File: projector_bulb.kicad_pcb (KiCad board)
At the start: 2 copper layers, 85.7 x 85.7 mm, 45 parts, among them J1 to_upright_+, J2 to_upright_-, J3 to_base, J4 Conn_02x02_Odd_Even, J5 Conn_02x02_Odd_Even, U1 PAM2863, U2 AP7381-33Y

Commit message: Added fillets after much blood sweat and tears
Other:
- board size 85.7 x 85.7 mm -> 85.7 x 85.6 mm

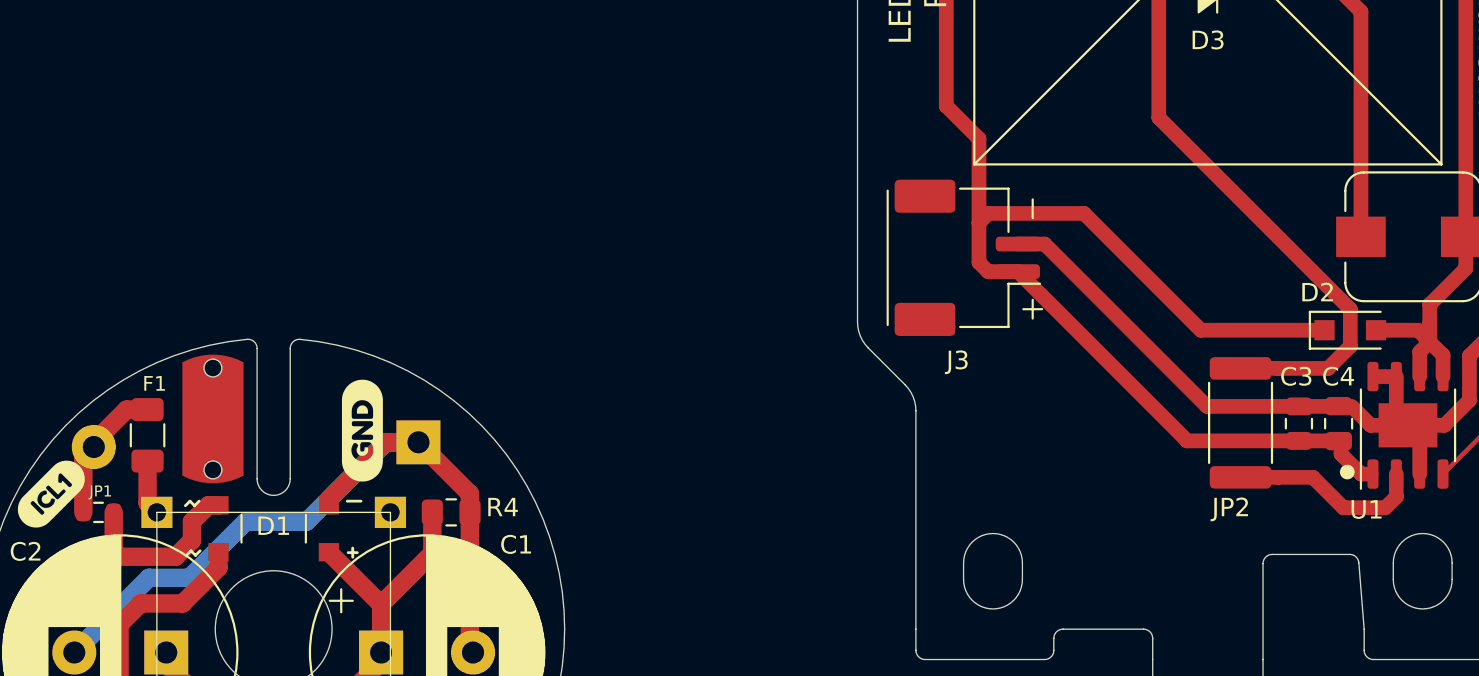
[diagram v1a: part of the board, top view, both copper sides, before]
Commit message: BOM and readme updated
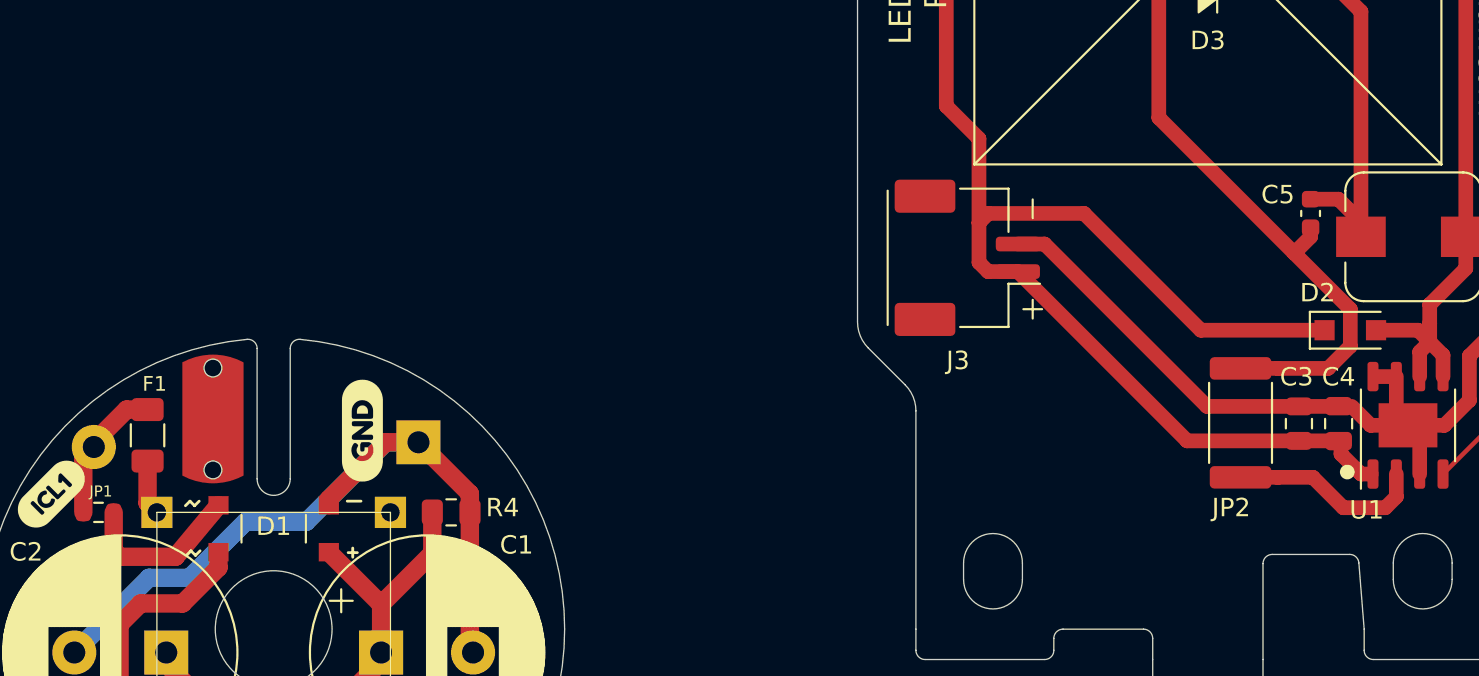
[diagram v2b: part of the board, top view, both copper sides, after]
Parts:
- added C5: 1μ, Capacitor_SMD:C_0603_1608Metric, F.Cu at (132.6, 53.6)
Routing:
- net Net-(C5-Pad1): track 35.6 -> 39.7 mm
- net Net-(C5-Pad2): track 58.3 -> 60.0 mm
- net Net-(D1-Pad3): track 31.0 -> 30.3 mm

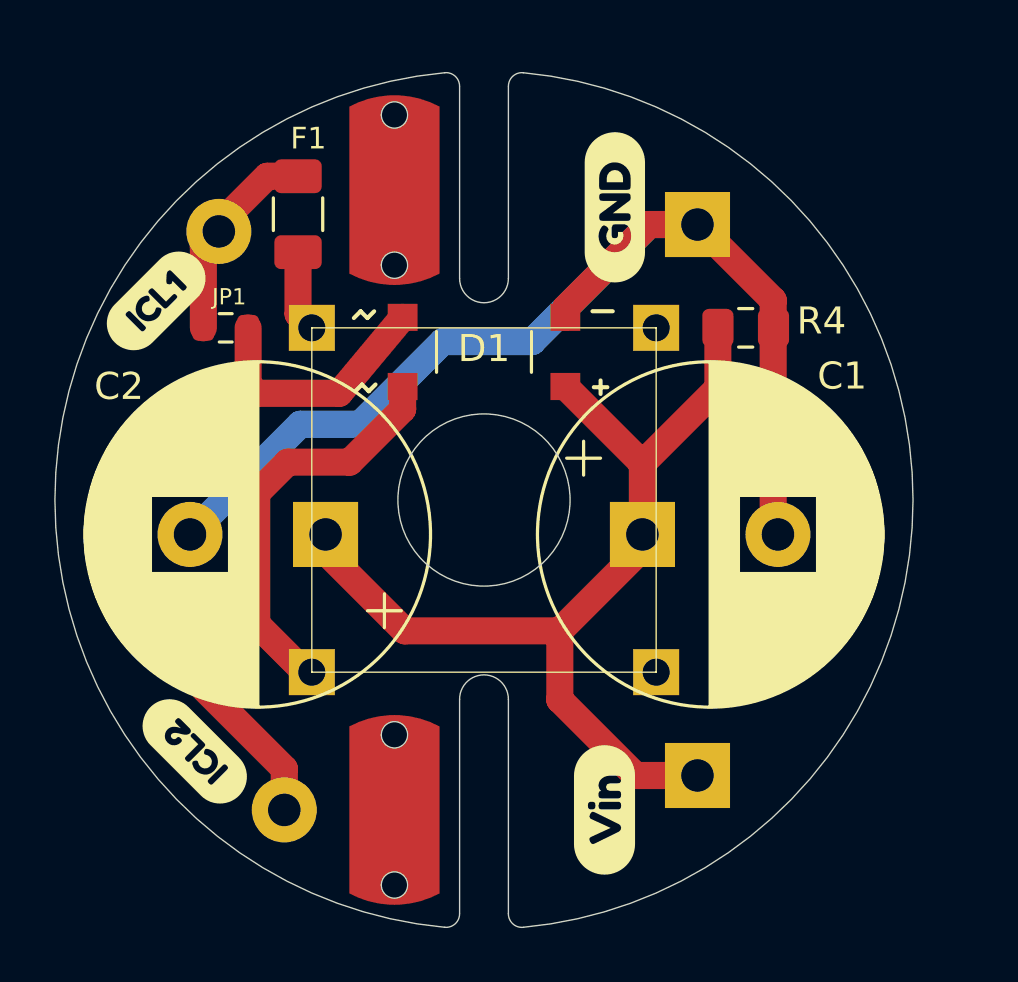
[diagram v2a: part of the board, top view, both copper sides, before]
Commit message: Locking in revision 3 finally; moved the optional ICL to a place where I can treat it like a test point
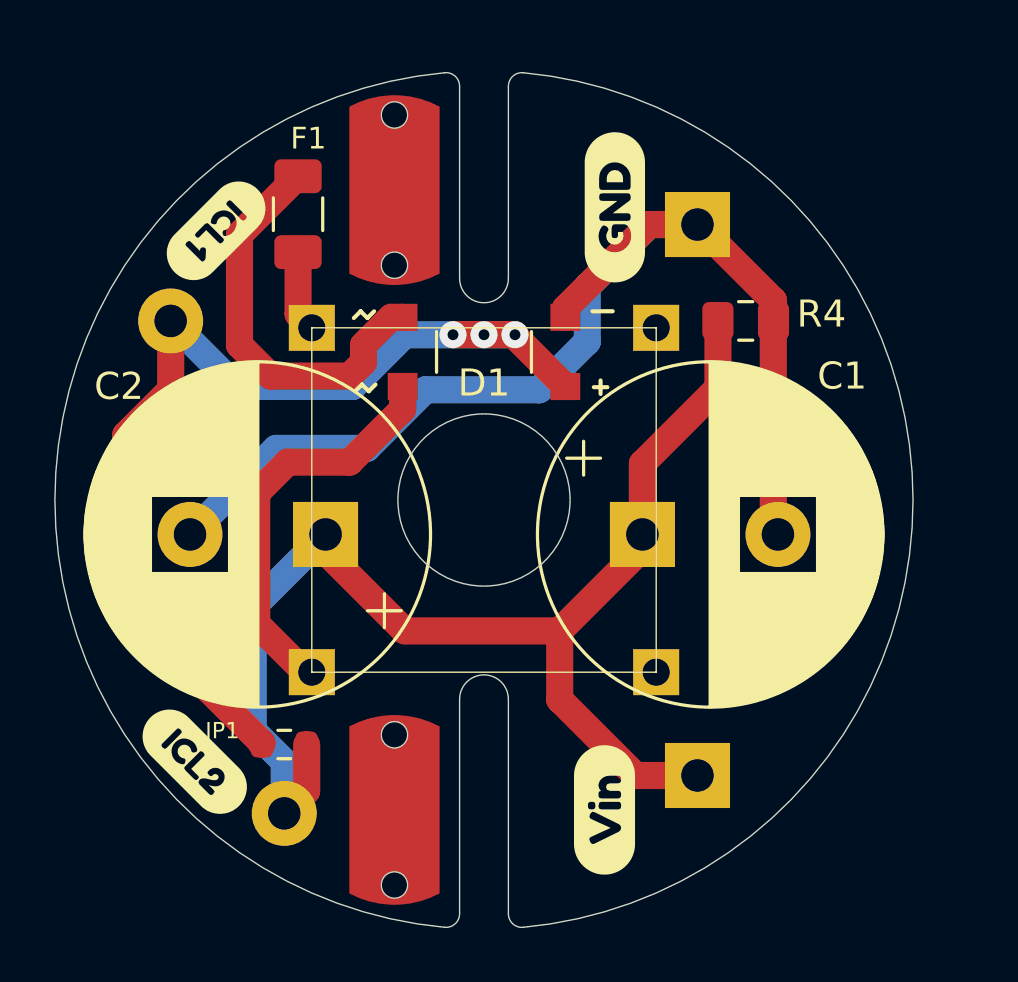
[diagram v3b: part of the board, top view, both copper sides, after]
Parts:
- moved JP1 15.5 mm to (68.8, 85.2)
- moved svg2mod 5.64 mm to (66.7, 65.2), turned to 180 degrees
- moved svg2mod 0.38 mm to (65.5, 85.9), turned to 270 degrees
- moved R4 0.25 mm to (85.9, 69.6)
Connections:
- D1 pad 1: VIN_BASE -> Net-(D1-Pad1)
- F1 pad 1: Net-(F1-Pad1) -> Net-(D1-Pad3)
- JP1 pad 1: Net-(F1-Pad1) -> Net-(D1-Pad1)
- JP1 pad 2: Net-(D1-Pad3) -> VIN_BASE
- TH1 pad 1: Net-(D1-Pad3) -> VIN_BASE
- TH1 pad 2: Net-(F1-Pad1) -> Net-(D1-Pad1)
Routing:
- net Net-(D1-Pad1): track 0.00 -> 37.8 mm, vias 0 -> 3
- net Net-(D1-Pad3): track 30.3 -> 14.9 mm
- net VIN_BASE: track 35.5 -> 46.5 mm
- net Net-(F1-Pad1): track 7.27 -> 0.00 mm
- net GND_BASE: track 42.6 -> 43.8 mm

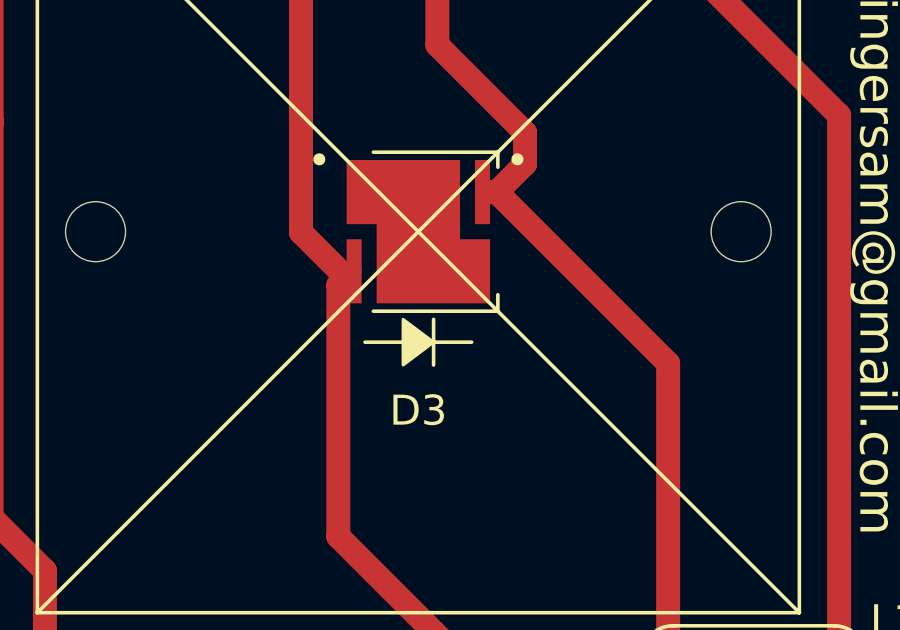
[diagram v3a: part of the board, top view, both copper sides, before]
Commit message: Add test point for thermal pad of LED
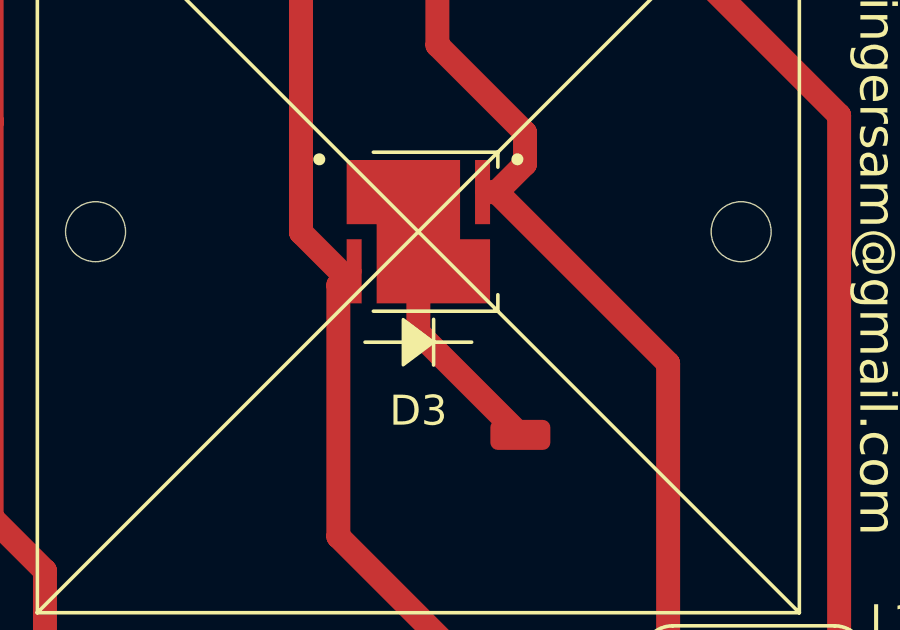
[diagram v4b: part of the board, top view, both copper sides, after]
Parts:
- added TP7: TestPoint, projector_bulb:Test_Point_0603, F.Cu at (130.4, 45.0)
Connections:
- D3 pad 3: (no net) -> Net-(D3-Pad3)
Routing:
- net Net-(D3-Pad3): track 0.00 -> 13.1 mm

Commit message: Changed all references of 7466310R to 7466313R
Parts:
- H1, H2: footprint projector_bulb:wuerth_7466310R -> projector_bulb:wuerth_7466313R
